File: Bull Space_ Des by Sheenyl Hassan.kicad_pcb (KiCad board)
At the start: 2 copper layers, 45 x 77 mm, 36 parts, among them IC1 TEENSY_4.0, IC2 XB24CZ7PIT-004, J1 Screw_Terminal_01x06, Q1 AOI21357, Q2 2N7002, Q3 2N7002, Q4 2N7002, Q5 AOI21357, U1 VXO7803-1000, U2 Flight-Computer_Adafruit_GPS_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

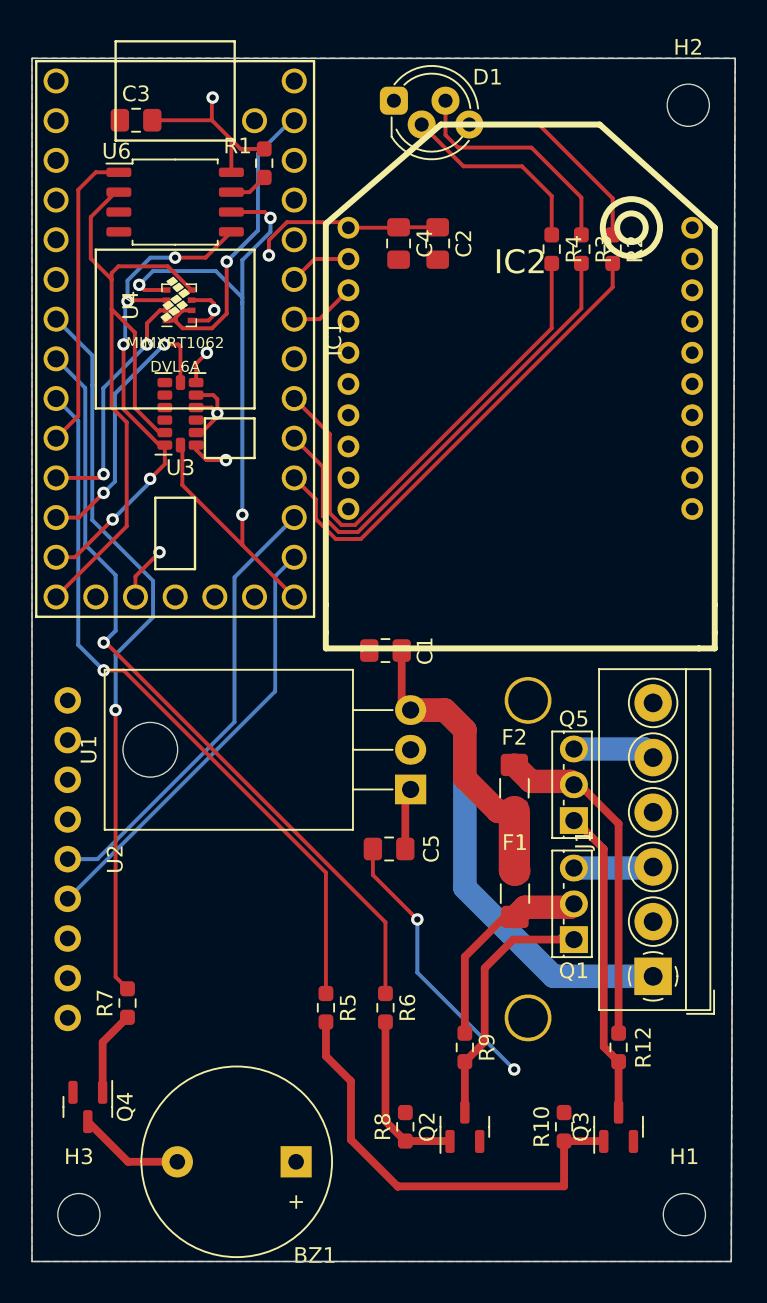
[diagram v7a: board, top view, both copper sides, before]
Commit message: Cleaned up bus lines, fixed stranded islands
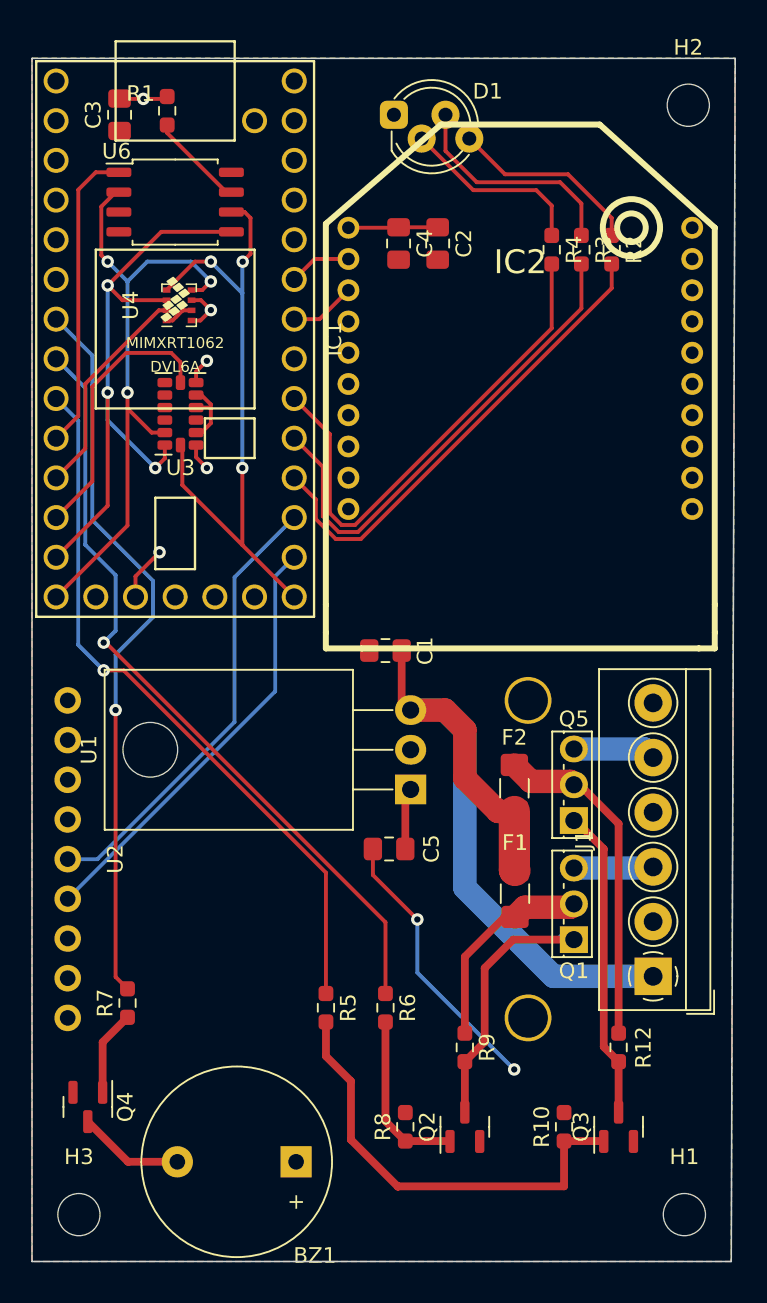
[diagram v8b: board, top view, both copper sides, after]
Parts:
- moved R1 7.06 mm to (80.7, 67.4)
- moved C3 1.11 mm to (77.6, 67.6), turned to 90 degrees
- moved D1 0.90 mm to (95.2, 67.6)
- moved R2 0.07 mm to (109.1, 76.2)
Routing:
- net GND: track 44.0 -> 24.5 mm, vias 4 -> 2
- net +3V3: track 40.4 -> 23.3 mm, vias 6 -> 5
- net /MOSI: track 33.2 -> 40.1 mm, vias 5 -> 3
- net /MISO: track 45.5 -> 40.0 mm, vias 0 -> 3
- net /SCK: track 46.6 -> 41.7 mm
- net Net-(R1-Pad2): track 2.49 -> 6.18 mm
- net /BMP-CS: track 15.6 -> 13.9 mm, vias 2 -> 0
- net Net-(D1-Pad4): track 13.5 -> 12.3 mm
- net /ADXL-CS: track 18.2 -> 17.4 mm, vias 2 -> 0
- net Net-(D1-Pad2): track 12.7 -> 12.0 mm
